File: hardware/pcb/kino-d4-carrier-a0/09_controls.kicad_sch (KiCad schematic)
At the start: 24 parts, among them J900 HAPTIC MOTOR, J901 COVER HALL SENSOR, J902 LOCAL SHUTTER, J903 REMOTE DRY CONTACT, J904 FUNCTION BUTTON, Q900 2N7002, U900 DRV2605LDGSR, U901 SN74LVC1G14DBVR

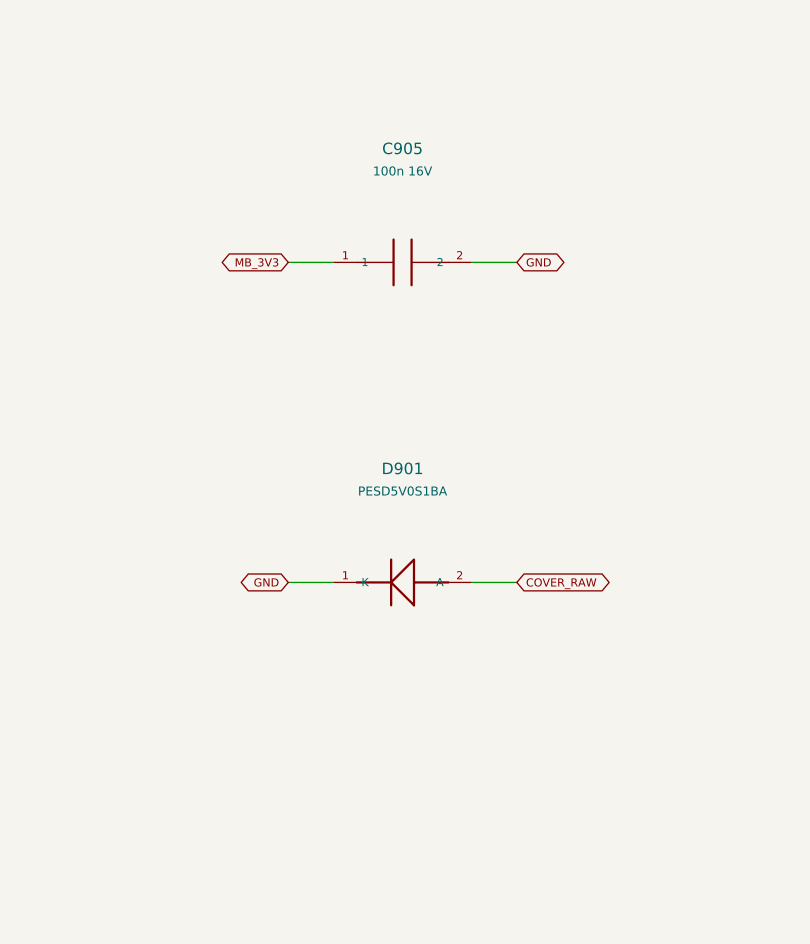
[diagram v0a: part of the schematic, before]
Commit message: feat(hardware): carrier A0.2 release pass - ready for fabrication with manual checks
Release review of the routed A0.2 carrier (A02-RELEASE.md: release matrix,
manual checks before ordering, bring-up tests). Final status: READY FOR
FABRICATION WITH SPECIFIC MANUAL CHECKS.

- USB-C input survives an unprogrammed STUSB4500 (20 V): D1001 SMF22A,
  R1004 10k, PD and load-switch P-FETs AO4409.
- Boost enable: R1204 100k BOOST_ENABLE to SYS_RAW (LTC2955-1 EN is a 2 uA
  source), Q1202 PMV16UN.
- I2C buffer U100 sides swapped (local bus on the TCA9517 A side's hard
  low); R100/R101 2.2k/22k hold EN low with JP1 pin 1 open.
- R105 SYNC_MASTER pull-down; D903 ESD on FN_N; TP1001 removed.
- SYS_RAW battery path as B.Cu and In2 pours with 25 extra vias; 1 oz inner
  copper in the stackup.
- XIAO socket pads get their solder-mask openings (footprint generator bug).
- Three fiducials per face; vias out of and away from pads; U1200 outline and
  pin-1 mark; legend lines and strokes 0.15 mm; silk association pass;
  CARRIER A0.2 / 2026-10 / S/N marking.
- Fab package (fab_a02.py): Gerbers + job file, drill, zip, placement files,
  fab BOM matched to LCSC by part number, hand-fit socket list, fab notes.
- Firmware constants header kino_carrier_a02.h.

DRC 0 / unconnected 0, ERC 0, verify.py --a02 passes.

Co-Authored-By: Claude Opus 5.5 <noreply@anthropic.com>
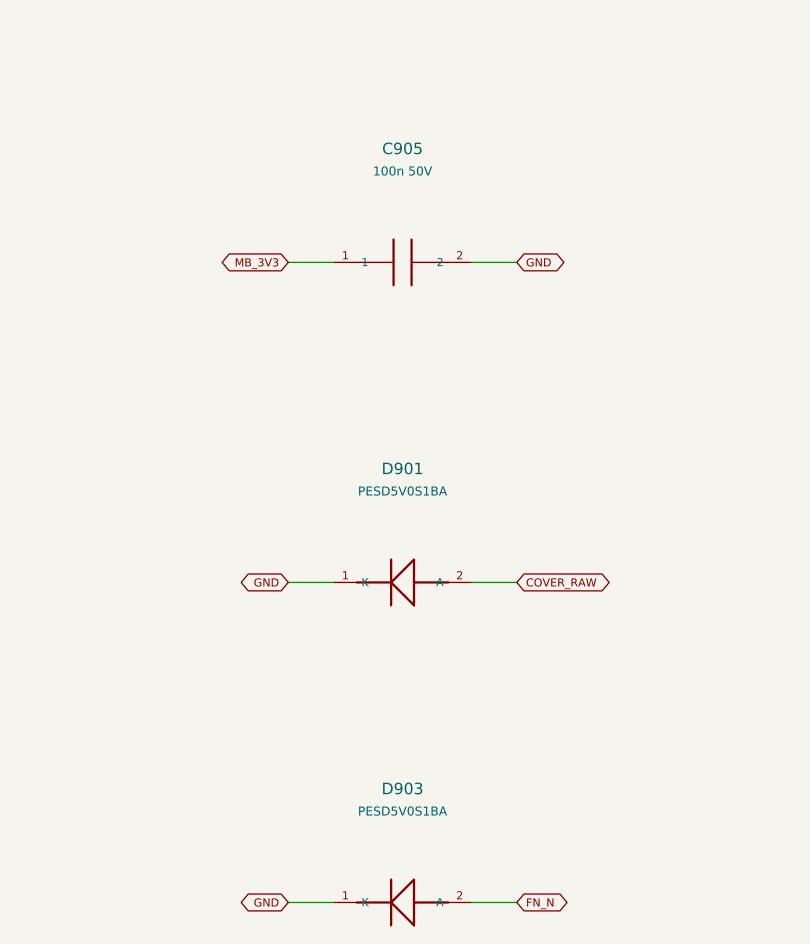
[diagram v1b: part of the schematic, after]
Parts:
- added D903: PESD5V0S1BA, Diode_SMD:D_SOD-323, symbol KINO_A0:D903
- C905: value 100n 16V -> 100n 50V
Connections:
- net FN_N: now also D903.2 (A)
- net GND: now also D903.1 (K)
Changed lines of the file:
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@@
                   (in_bom yes) (on_board yes) (dnp no)
                   (property "Reference" "C905" (at 73.66 185.5 0) (effects (font (size 1.27 1.27))))
-                  (property "Value" "100n 16V" (at 73.66 188.0 0) (effects (font (size 1.0 1.0))))
+                  (property "Value" "100n 50V" (at 73.66 188.0 0) (effects (font (size 1.0 1.0))))
                   (property "Footprint" "Capacitor_SMD:C_0603_1608Metric" (at 73.66 198.12 0) (effects (font (size 1 1)) (hide yes)))
                   (property "Datasheet" "https://www.yageogroup.com/component-documentation/download/specsheet/CC0603KRX7R9BB104" (at 73.66 198.12 0) (effects (font (size 1 1)) (hide yes)))
@@
                     (effects (font (size 0.9 0.9)) (justify left))
                     (property "Intersheetrefs" "${INTERSHEET_REFS}" (at 490.21999999999997 233.68 180) (effects (font (size 0.8 0.8)) (hide yes))))
+(symbol (lib_id "KINO_A0:D903") (at 73.66 269.24 0) (unit 1)
+                  (in_bom yes) (on_board yes) (dnp no)
+                  (property "Reference" "D903" (at 73.66 256.62 0) (effects (font (size 1.27 1.27))))
+                  (property "Value" "PESD5V0S1BA" (at 73.66 259.12 0) (effects (font (size 1.0 1.0))))
+                  (property "Footprint" "Diode_SMD:D_SOD-323" (at 73.66 269.24 0) (effects (font (size 1 1)) (hide yes)))
+                  (property "Datasheet" "https://assets.nexperia.com/documents/data-sheet/PESD5V0S1BA.pdf" (at 73.66 269.24 0) (effects (font (size 1 1)) (hide yes)))
+                  (property "Design note" "Cased button line, same class as the shutter input (D902). Beside J904." (at 73.66 269.24 0) (effects (font (size 1 1)) (hide yes)))
+                  (pin "1")(pin "2")
+                  (instances (project "KINO_D4_Carrier_A0" (path "/3e6ce248-02da-5043-9ed8-b7ca2a49de29/c327de22-5c04-5d62-b574-57593a1d0d4b" (reference "D903") (unit 1)))))
+(wire (pts (xy 66.03999999999999 269.24) (xy 60.959999999999994 269.24)) (stroke (width 0) (type default)))
+(global_label "GND" (shape bidirectional) (at 60.959999999999994 269.24 0)
+                    (effects (font (size 0.9 0.9)) (justify right))
+                    (property "Intersheetrefs" "${INTERSHEET_REFS}" (at 60.959999999999994 269.24 0) (effects (font (size 0.8 0.8)) (hide yes))))
+(wire (pts (xy 81.28 269.24) (xy 86.36 269.24)) (stroke (width 0) (type default)))
+(global_label "FN_N" (shape bidirectional) (at 86.36 269.24 180)
+                    (effects (font (size 0.9 0.9)) (justify left))
+                    (property "Intersheetrefs" "${INTERSHEET_REFS}" (at 86.36 269.24 180) (effects (font (size 0.8 0.8)) (hide yes))))
 (embedded_fonts no))
